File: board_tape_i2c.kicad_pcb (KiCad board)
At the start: 2 copper layers, 40.5 x 56.6 mm, 27 parts, among them J1 C64-CassettePort, J10 - 5V power out Power for external devices, J2 Conn_01x04_Socket, J3 Conn_01x04_Socket, J4 Conn_01x04_Socket, J5 Conn_01x04_Socket, J6 Conn_01x04, J7 Conn_01x04, J8 Conn_01x04, J9 Conn_01x04, Q1 BSS138W, Q2 BSS138W, U1 XC6206P332MR

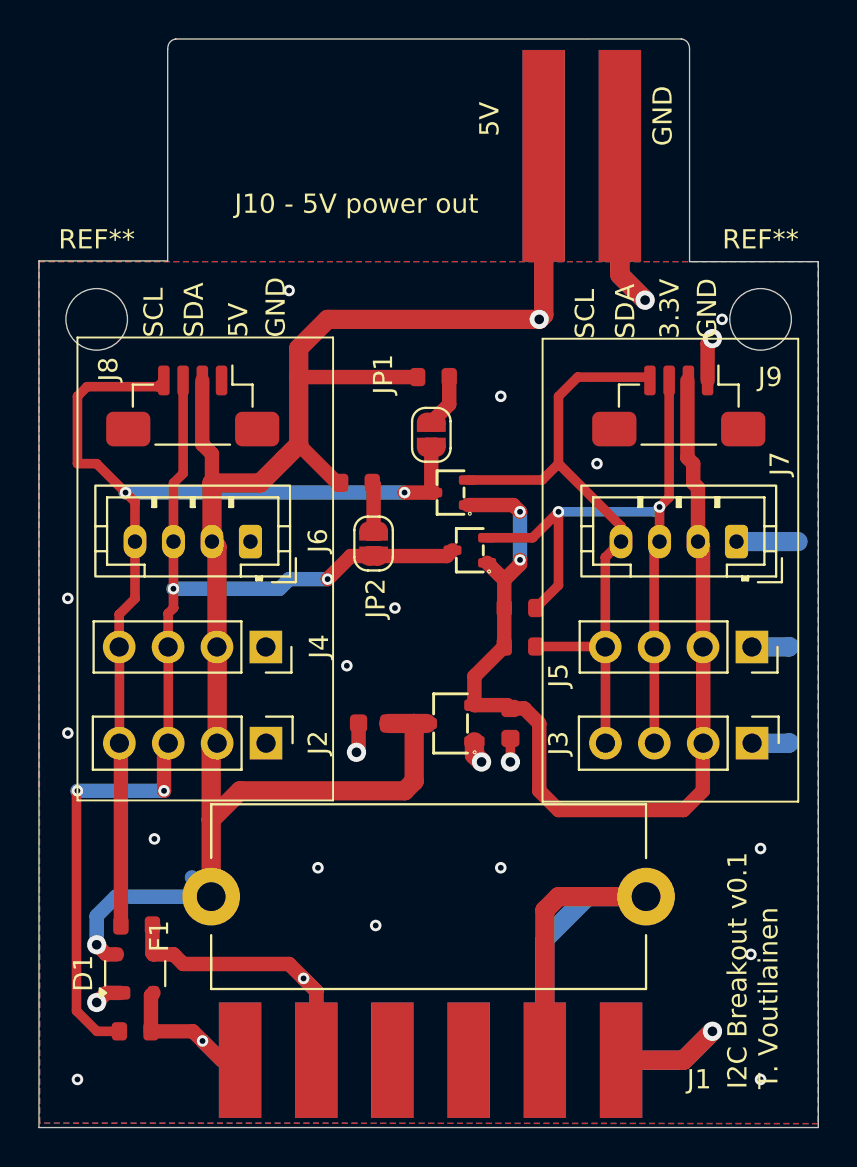
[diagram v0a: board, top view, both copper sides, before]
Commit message: Version 0.2
SDA and SCL reversed in cassette port

Signed-off-by: Timo Voutilainen <voutti@users.noreply.github.com>
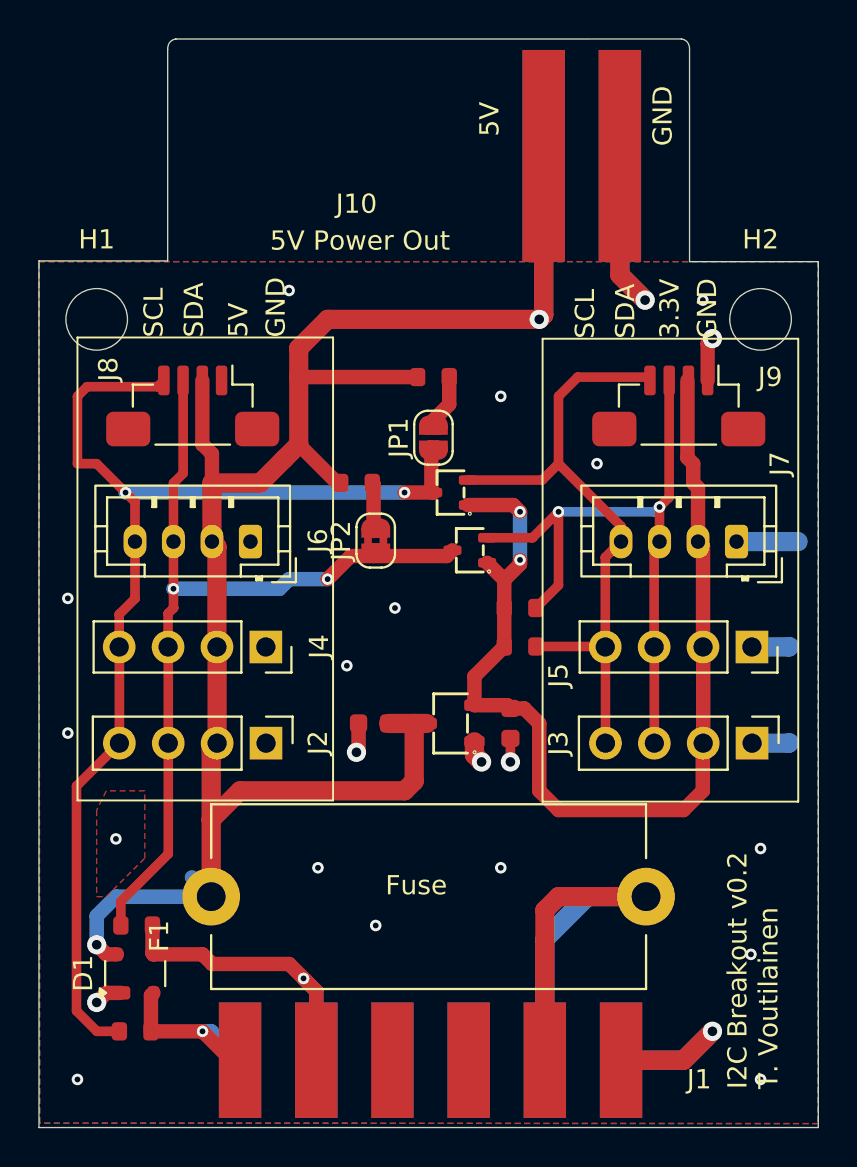
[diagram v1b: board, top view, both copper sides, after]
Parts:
- removed REF** (x2): MountingHole_3.2mm_M3, MountingHole:MountingHole_3.2mm_M3
- added H1: MountingHole, TiVo_Library:MountingHole_3.2mm_M3_Reduced, F.Cu at (136.6, 112.0)
- added H2: MountingHole, TiVo_Library:MountingHole_3.2mm_M3_Reduced, F.Cu at (171.1, 112.0)
- J10: renamed from J10 - 5V power out
- JP2: value SolderJumper_2_Open -> SolderJumper_2_Bridged; footprint Jumper:SolderJumper-2_P1.3mm_Open_RoundedPad1.0x1.5mm -> Jumper:SolderJumper-2_P1.3mm_Bridged2Bar_RoundedPad1.0x1.5mm
- R1, R2, R3, R4: value 4k7 -> 10k
- moved JP1 0.19 mm to (154.1, 118.2)
- moved JP2 0.19 mm to (151.1, 123.5)
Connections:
- R7 pad 2: SCL_5V -> SDA_5V
- R8 pad 2: SDA_5V -> SCL_5V
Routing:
- net SDA_5V: track 55.7 -> 45.0 mm, vias 4 -> 2
- net SCL_5V: track 52.9 -> 61.0 mm
- net GND: vias 23 -> 22
- net (no net): vias 0 -> 1
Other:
- board text added: "5V Power Out"
- board text added: "Fuse"
- board text added: "I2C Breakout v0.2 T. Voutilainen"
- board text removed: "I2C Breakout v0.1 T. Voutilainen"
